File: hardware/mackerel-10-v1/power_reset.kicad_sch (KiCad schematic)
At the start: 27 parts, among them J10 Conn_02x03_Odd_Even, J11 Conn_02x03_Odd_Even, J6 Barrel_Jack_MountingPin, J8 Conn_02x03_Odd_Even, SW1 SW_Push, U15 LM2576T-5, U16 NE555P, U17 AMS1117-3.3

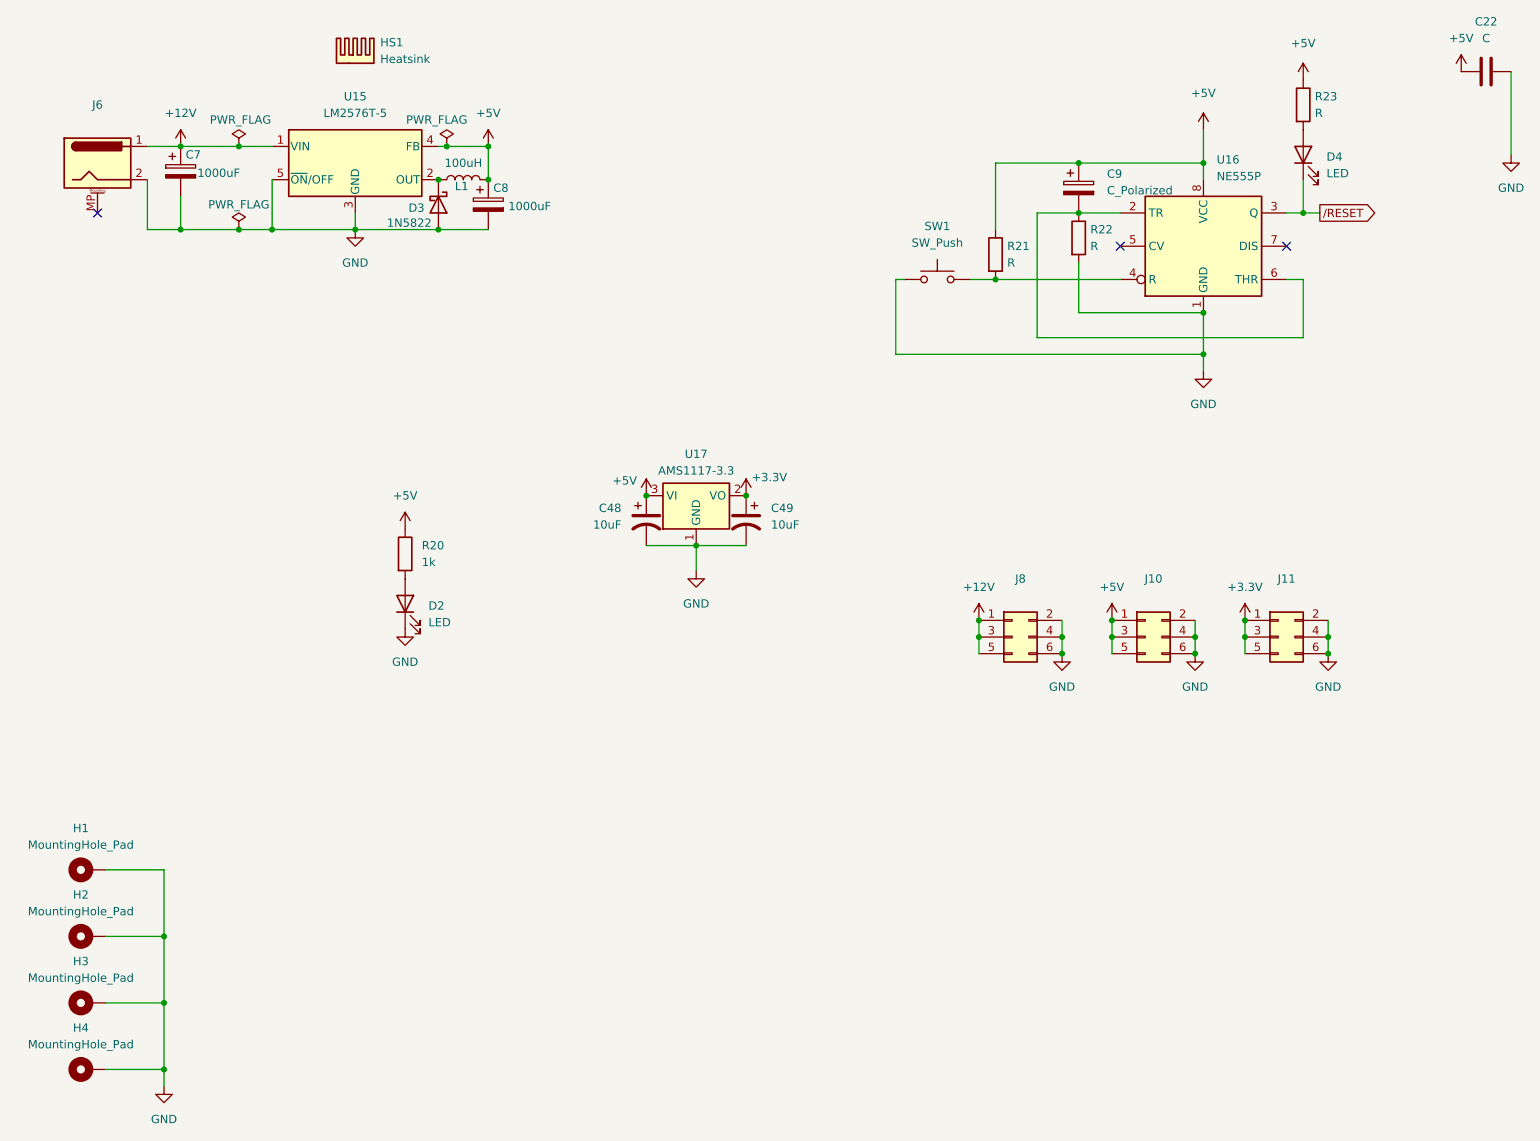
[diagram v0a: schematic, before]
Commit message: Remove BERR from CPLD
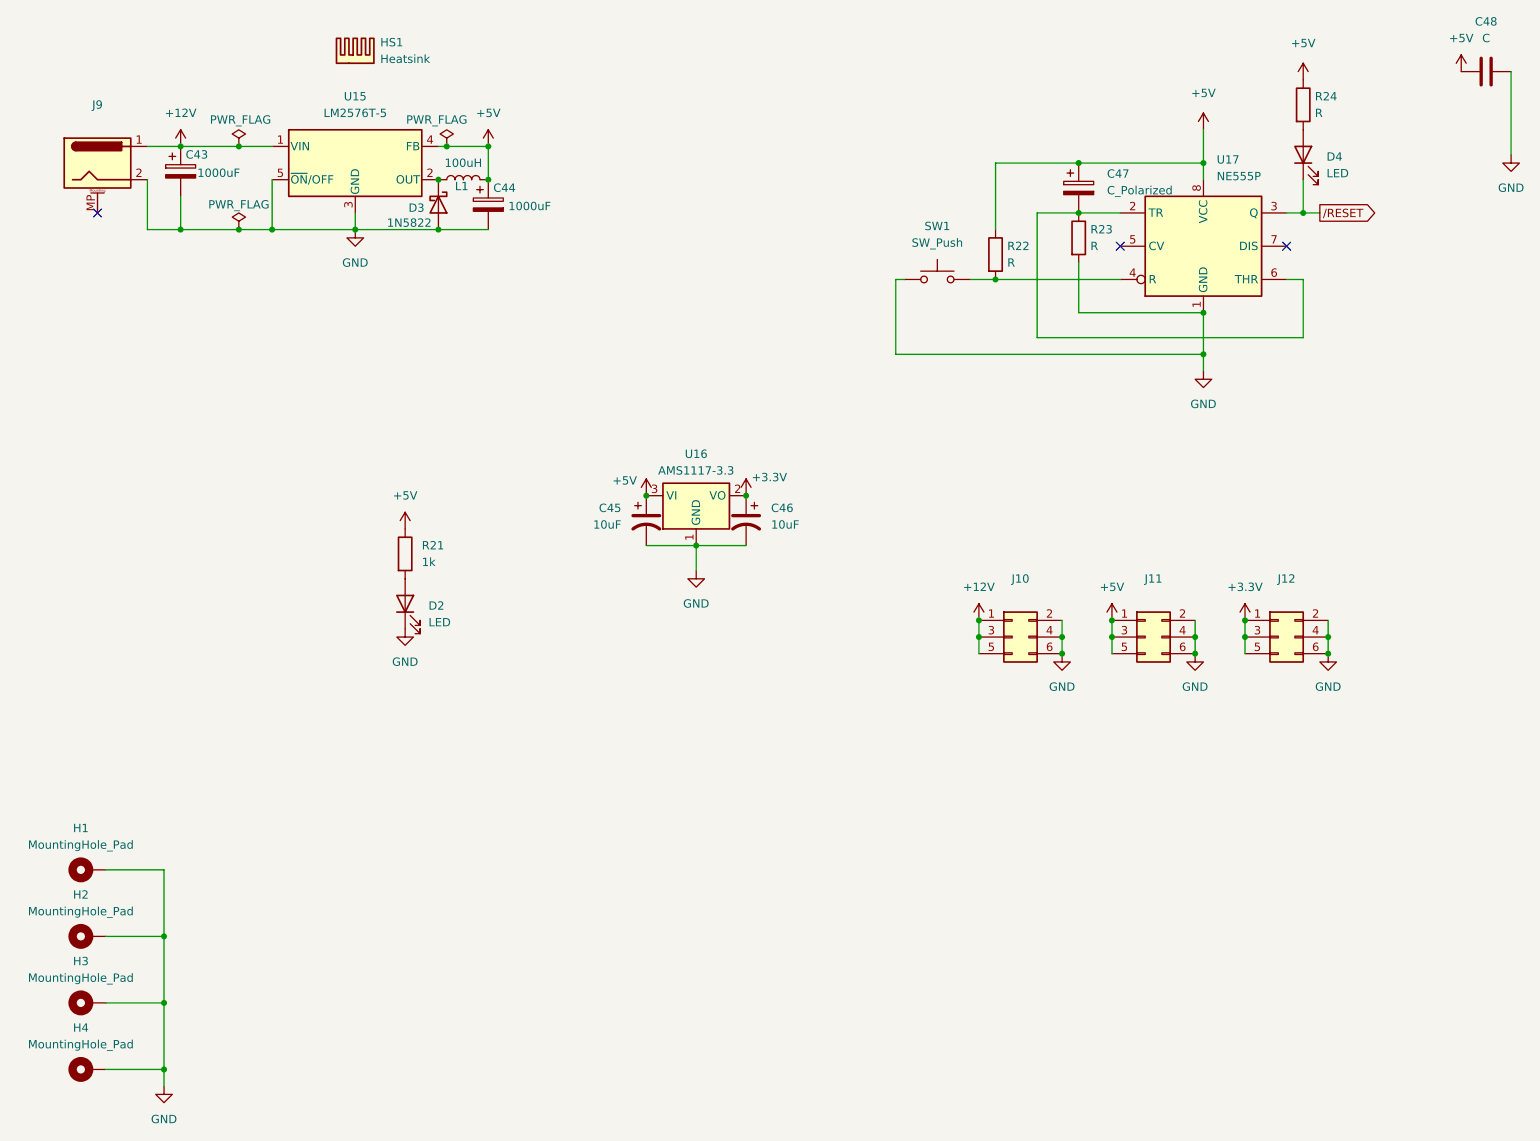
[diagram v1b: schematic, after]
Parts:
- renumbered C7 to C43, C8 to C44, C48 to C45, C49 to C46, C9 to C47, C22 to C48, J8 to J10, J10 to J11, J11 to J12, J6 to J9, R20 to R21, R21 to R22, R22 to R23, R23 to R24, U17 to U16, U16 to U17

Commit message: Mackerel-10 v1.1 release PCB
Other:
- title: Mackerel-10 SBC v1 -> Mackerel-10 SBC v1.1
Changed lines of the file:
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@@
 	(paper "A")
 	(title_block
-		(title "Mackerel-10 SBC v1")
-		(date "2024-09-23")
-		(rev "1.0a")
+		(title "Mackerel-10 SBC v1.1")
+		(date "2024-10-27")
+		(rev "1.1a")
 		(company "Colin Maykish")
 	)

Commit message: Add Mackerel-10 v1.1 BOM
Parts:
- C47: value C_Polarized -> 10uF
- C48: value C -> 0.1uF
- R22, R23: value R -> 10k
- R24: value R -> 1k
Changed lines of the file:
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@@
 			)
 		)
-		(property "Value" "C_Polarized"
+		(property "Value" "10uF"
 			(at 188.468 49.9109 0)
 			(effects
@@
 			)
 		)
-		(property "Value" "R"
+		(property "Value" "1k"
 			(at 220.218 38.0999 0)
 			(effects
@@
 			)
 		)
-		(property "Value" "R"
+		(property "Value" "10k"
 			(at 173.228 60.9599 0)
 			(effects
@@
 			)
 		)
-		(property "Value" "R"
+		(property "Value" "10k"
 			(at 185.928 58.4199 0)
 			(effects
@@
 			)
 		)
-		(property "Value" "C"
+		(property "Value" "0.1uF"
 			(at 246.38 26.67 90)
 			(effects

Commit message: Mackerel-10 v1.2 Gerber release
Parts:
- removed C47: 10uF, Capacitor_THT:CP_Radial_D5.0mm_P2.50mm, symbol Device:C_Polarized
- removed C48: 0.1uF, Capacitor_THT:C_Disc_D4.3mm_W1.9mm_P5.00mm, symbol Device:C
- removed R23: 10k, Resistor_THT:R_Axial_DIN0207_L6.3mm_D2.5mm_P7.62mm_Horizontal, symbol Device:R
- removed R24: 1k, Resistor_THT:R_Axial_DIN0207_L6.3mm_D2.5mm_P7.62mm_Horizontal, symbol Device:R
- removed U17: NE555P, Package_DIP:DIP-8_W7.62mm, symbol Timer:NE555P
- added C47: 0.01uF, Capacitor_THT:C_Disc_D4.3mm_W1.9mm_P5.00mm, symbol Device:C
- added U17: DS1233, Package_TO_SOT_THT:TO-92L_Inline, symbol mackerel-68k-symbols:DS1233
- R22: value 10k -> 1k
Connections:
- net +5V: now also U17.3 (VCC)
- net GND: now also SW1.2, C47.2, U17.1 (GND); no longer SW1.1
- net /RESET: now also SW1.1, C47.1, U17.2 (/RESET)
- net at R22.2: now also D4.2 (A); no longer SW1.2
- no-connect marks 3 -> 1
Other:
- title: Mackerel-10 SBC v1.1 -> Mackerel-10
